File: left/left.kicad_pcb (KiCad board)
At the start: 2 copper layers, 163.9 x 104.5 mm, 51 parts, among them J1 Modulo-Jack, J2 Modulo-Jack, J3 Modulo-Jack, SW1 SW_Push, SW10 SW_Push, SW11 SW_Push, SW12 SW_Push, SW13 SW_Push, SW14 SW_Push, SW15 SW_Push, SW16 SW_Push, SW17 SW_Push, SW18 SW_Push, SW19 SW_Push, SW2 SW_Push, SW20 SW_Push, SW21 SW_Push, SW22 SW_Push, SW23 SW_Push, SW24 SW_Push, SW25 SW_Push, SW26 SW_Push, SW27 SW_Push, SW28 SW_Push, SW29 SW_Push, SW3 SW_Push, SW30 SW_Push, SW31 SW_Push, SW32 SW_SPDT, SW33 SW_SPDT, SW4 SW_Push, SW5 SW_Push, SW6 SW_Push, SW7 SW_Push, SW8 SW_Push, SW9 SW_Push, U1 MCP23017_SP, U2 MCP23017_SP

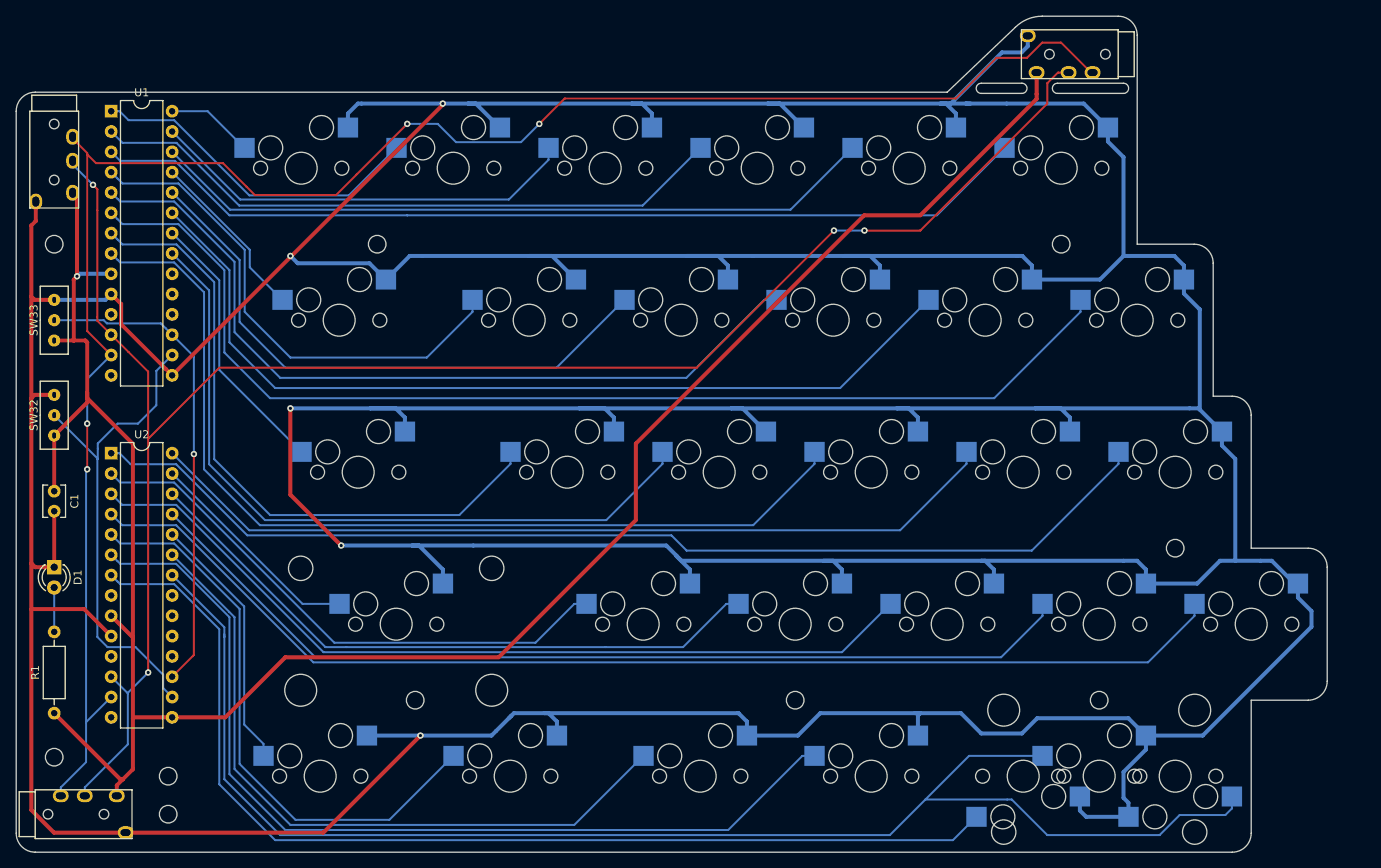
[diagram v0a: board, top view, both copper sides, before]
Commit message: left: change address switch to DPDT
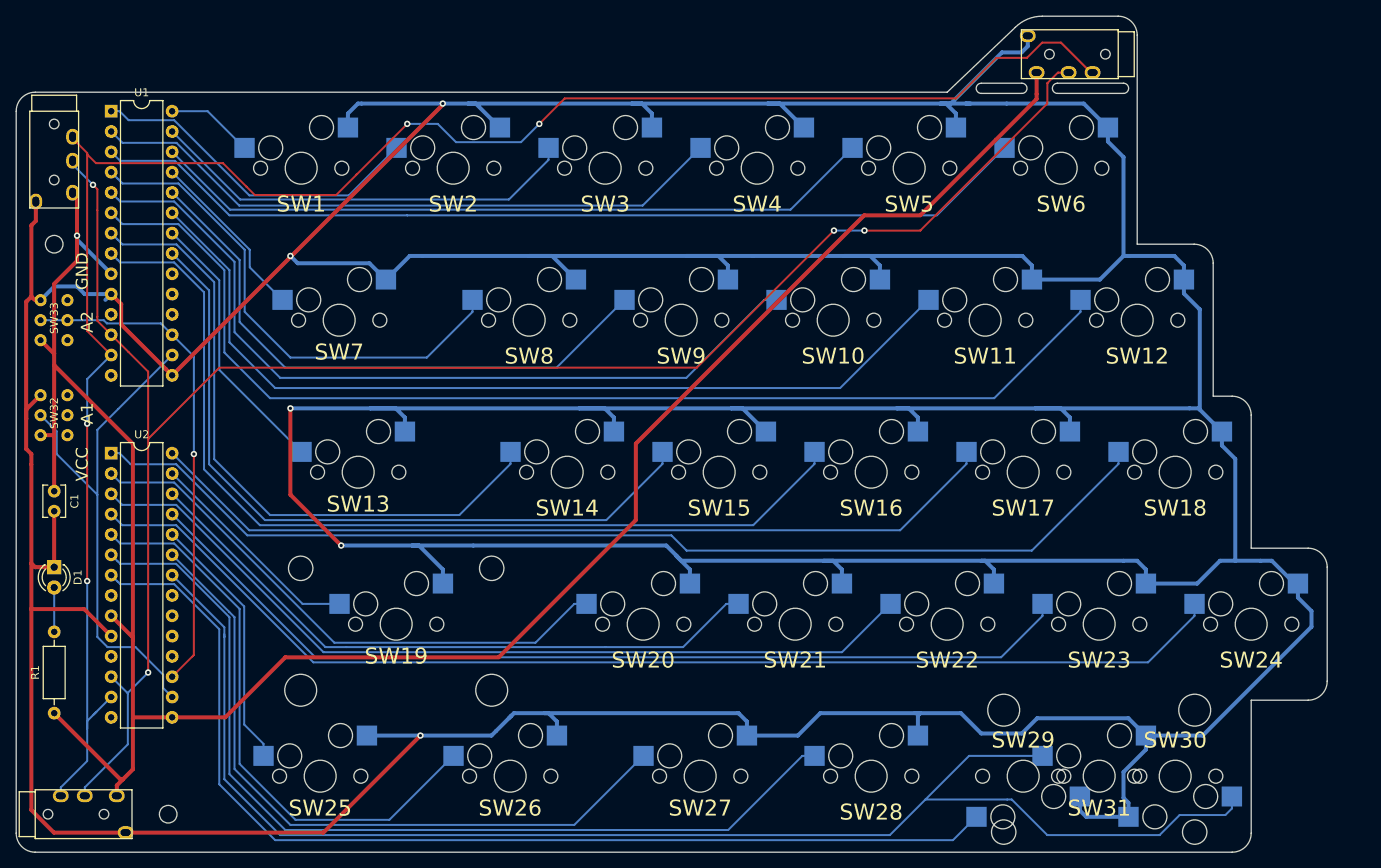
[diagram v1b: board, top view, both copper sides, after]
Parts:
- removed the ? at (190.0, 133.0)
- removed the ? at (59.4, 140.1)
- removed the ? at (73.6, 142.5)
- removed the ? at (104.5, 133.0)
- removed the ? at (99.8, 76.0)
- removed the ? at (185.2, 76.0)
- removed the ? at (199.5, 114.0)
- removed the ? at (152.0, 133.0)
- SW32, SW33: value SW_SPDT -> SW_DPDT_x2; footprint lib:SlideSwitch_SS-12D00 -> lib:SlideSwitch_IS2235
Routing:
- net VCC: track 271.5 -> 278.3 mm
- net A1: track 61.7 -> 65.4 mm
- net GND: track 1029.5 -> 1031.7 mm
- net A2: track 60.5 -> 62.2 mm
- net SDA: track 230.5 -> 231.7 mm
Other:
- board text added: "A1"
- board text added: "A2"
- board text added: "GND"
- board text added: "VCC"

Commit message: left: ネジ穴を再生
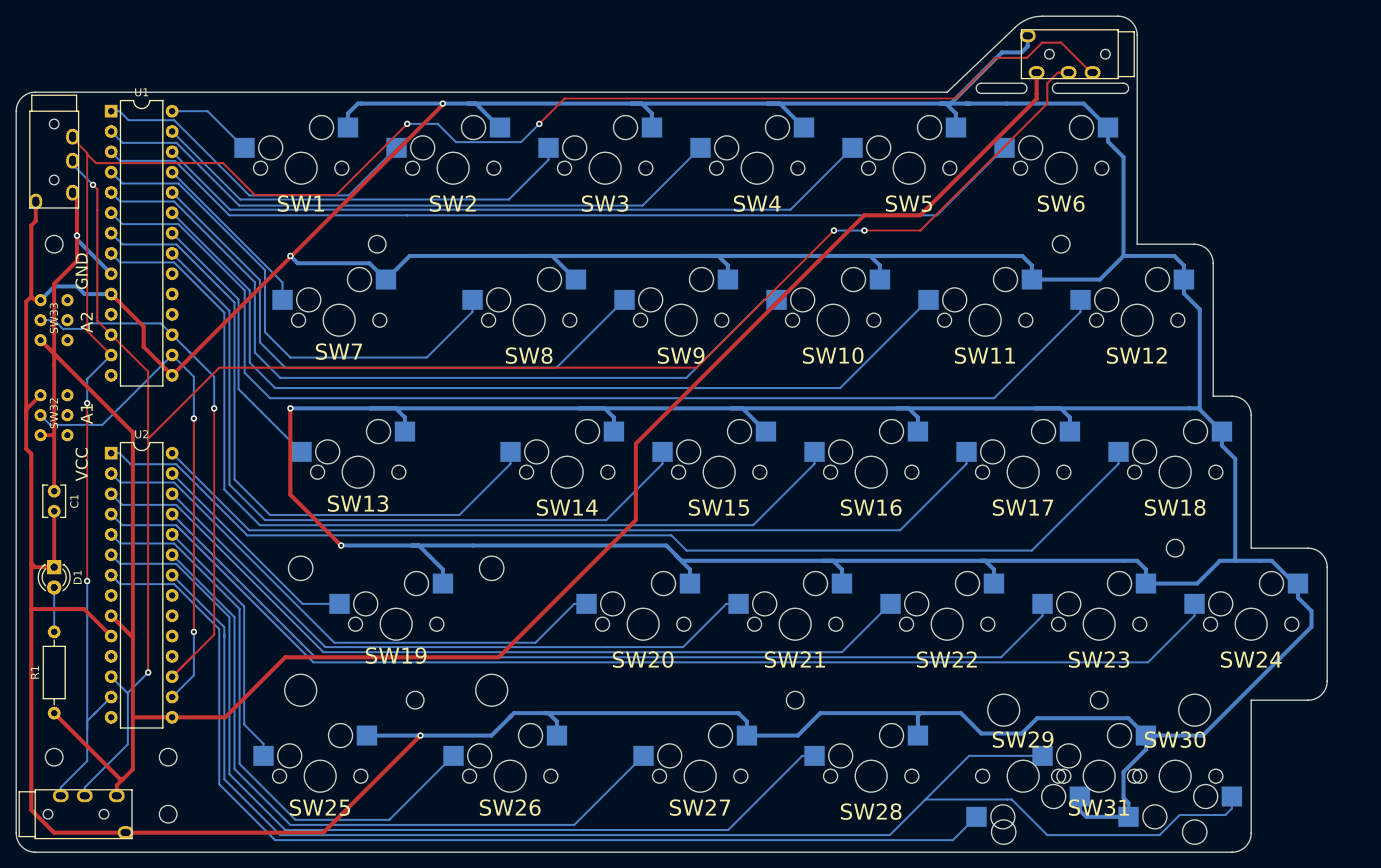
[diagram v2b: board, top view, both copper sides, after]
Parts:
- added ?: M2, lib:MountingHole_2.2mm_M2, F.Cu at (190.0, 133.0)
- added ?: M2, lib:MountingHole_2.2mm_M2, F.Cu at (185.2, 76.0)
- added ?: M2, lib:MountingHole_2.2mm_M2, F.Cu at (199.5, 114.0)
- added ?: M2, lib:MountingHole_2.2mm_M2, F.Cu at (152.0, 133.0)
- added ?: M2, lib:MountingHole_2.2mm_M2, F.Cu at (104.5, 133.0)
- added ?: M2, lib:MountingHole_2.2mm_M2, F.Cu at (99.8, 76.0)
- added ?: M2, lib:MountingHole_2.2mm_M2, F.Cu at (59.4, 140.1)
- added ?: M2, lib:MountingHole_2.2mm_M2, F.Cu at (73.6, 140.1)
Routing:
- net A2: track 62.2 -> 69.5 mm
- net VCC: track 278.3 -> 282.4 mm
- net GND: track 1031.7 -> 1030.7 mm
- net A1: track 65.4 -> 65.6 mm, vias 0 -> 2

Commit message: last commit
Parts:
- added ?: M2, lib:MountingHole_2.2mm_M2, F.Cu at (78.4, 61.8)
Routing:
- net SW1: track 10.9 -> 12.3 mm
- net GND: track 1030.7 -> 1030.2 mm
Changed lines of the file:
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@@
     (thickness 1.6)
     (drawings 37)
-    (tracks 549)
+    (tracks 550)
     (zones 0)
-    (modules 51)
+    (modules 52)
     (nets 56)
   )
@@
   )
   (module lib:MountingHole_2.2mm_M2 locked (layer F.Cu)
+    (at 78.375 61.75)
+    (descr "Mounting Hole 2.2mm, no annular, M2")
+    (tags "mounting hole 2.2mm no annular m2")
+    (attr virtual)
+    (fp_text reference "" (at 0 -3.2) (layer F.SilkS)
+      (effects (font (size 1 1) (thickness 0.15)))
+    )
+    (fp_text value M2 (at 0 3.2) (layer F.Fab)
+      (effects (font (size 1 1) (thickness 0.15)))
+    )
+    (fp_circle (center 0 0) (end 1.75 0) (layer F.CrtYd) (width 0.05))
+    (fp_text user %R (at 0.3 0) (layer F.Fab)
+      (effects (font (size 1 1) (thickness 0.15)))
+    )
+    (pad 1 np_thru_hole circle (at 0 0) (size 2.2 2.2) (drill 2.2) (layers *.Cu *.Mask))
+  )
+  (module lib:MountingHole_2.2mm_M2 locked (layer F.Cu)
     (at 190 133)
     (descr "Mounting Hole 2.2mm, no annular, M2")
@@
   (segment (start 56.515 146.719002) (end 56.515 121.61) (width 0.5) (layer F.Cu) (net 1))
   (segment (start 59.375 109.375) (end 59.375 116.375) (width 0.5) (layer F.Cu) (net 1))
-  (segment (start 214.842 120.17) (end 214.842 118.42) (width 0.5) (layer B.Cu) (net 1))
-  (segment (start 216.535 121.863) (end 214.842 120.17) (width 0.5) (layer B.Cu) (net 1))
-  (segment (start 216.535 123.825) (end 216.535 121.863) (width 0.5) (layer B.Cu) (net 1))
-  (segment (start 195.842 137.42) (end 202.94 137.42) (width 0.5) (layer B.Cu) (net 1))
-  (segment (start 202.94 137.42) (end 216.535 123.825) (width 0.5) (layer B.Cu) (net 1))
   (segment (start 188.067 58.42) (end 178.435 58.42) (width 0.5) (layer B.Cu) (net 1))
   (segment (start 191.067 61.42) (end 188.067 58.42) (width 0.5) (layer B.Cu) (net 1))
@@
   (segment (start 66.5 82.235) (end 70.555 86.29) (width 0.5) (layer F.Cu) (net 1))
   (segment (start 70.555 88.83) (end 73.320001 91.595001) (width 0.5) (layer F.Cu) (net 1))
+  (segment (start 214.842 120.17) (end 214.842 118.42) (width 0.5) (layer B.Cu) (net 1))
+  (segment (start 215.9 121.228) (end 214.842 120.17) (width 0.5) (layer B.Cu) (net 1))
+  (segment (start 215.9 124.46) (end 215.9 121.228) (width 0.5) (layer B.Cu) (net 1))
+  (segment (start 202.94 137.42) (end 215.9 124.46) (width 0.5) (layer B.Cu) (net 1))
+  (segment (start 195.842 137.42) (end 202.94 137.42) (width 0.5) (layer B.Cu) (net 1))
   (segment (start 67.2 143.65) (end 67.2 144.95) (width 0.5) (layer F.Cu) (net 2))
   (segment (start 69.215 135.255) (end 69.325 135.145) (width 0.5) (layer F.Cu) (net 2))
@@
   (segment (start 160.655 74.295) (end 167.64 74.295) (width 0.25) (layer F.Cu) (net 4))
   (segment (start 167.64 74.295) (end 183.515 58.42) (width 0.25) (layer F.Cu) (net 4))
-  (segment (start 78.555 59.375) (end 74.12 59.375) (width 0.25) (layer B.Cu) (net 5))
-  (segment (start 83.165 63.96) (end 83.14 63.96) (width 0.25) (layer B.Cu) (net 5))
-  (segment (start 83.14 63.96) (end 78.555 59.375) (width 0.25) (layer B.Cu) (net 5))
+  (segment (start 83.165 63.96) (end 83.165 61.615) (width 0.25) (layer B.Cu) (net 5))
+  (segment (start 80.925 59.375) (end 77.79 59.375) (width 0.25) (layer B.Cu) (net 5))
+  (segment (start 83.165 61.615) (end 80.925 59.375) (width 0.25) (layer B.Cu) (net 5))
+  (segment (start 77.79 59.375) (end 74.12 59.375) (width 0.25) (layer B.Cu) (net 5))
   (segment (start 102.14 63.96) (end 102.165 63.96) (width 0.25) (layer B.Cu) (net 6))
   (segment (start 66.5 59.375) (end 67.55 59.375) (width 0.25) (layer B.Cu) (net 6))

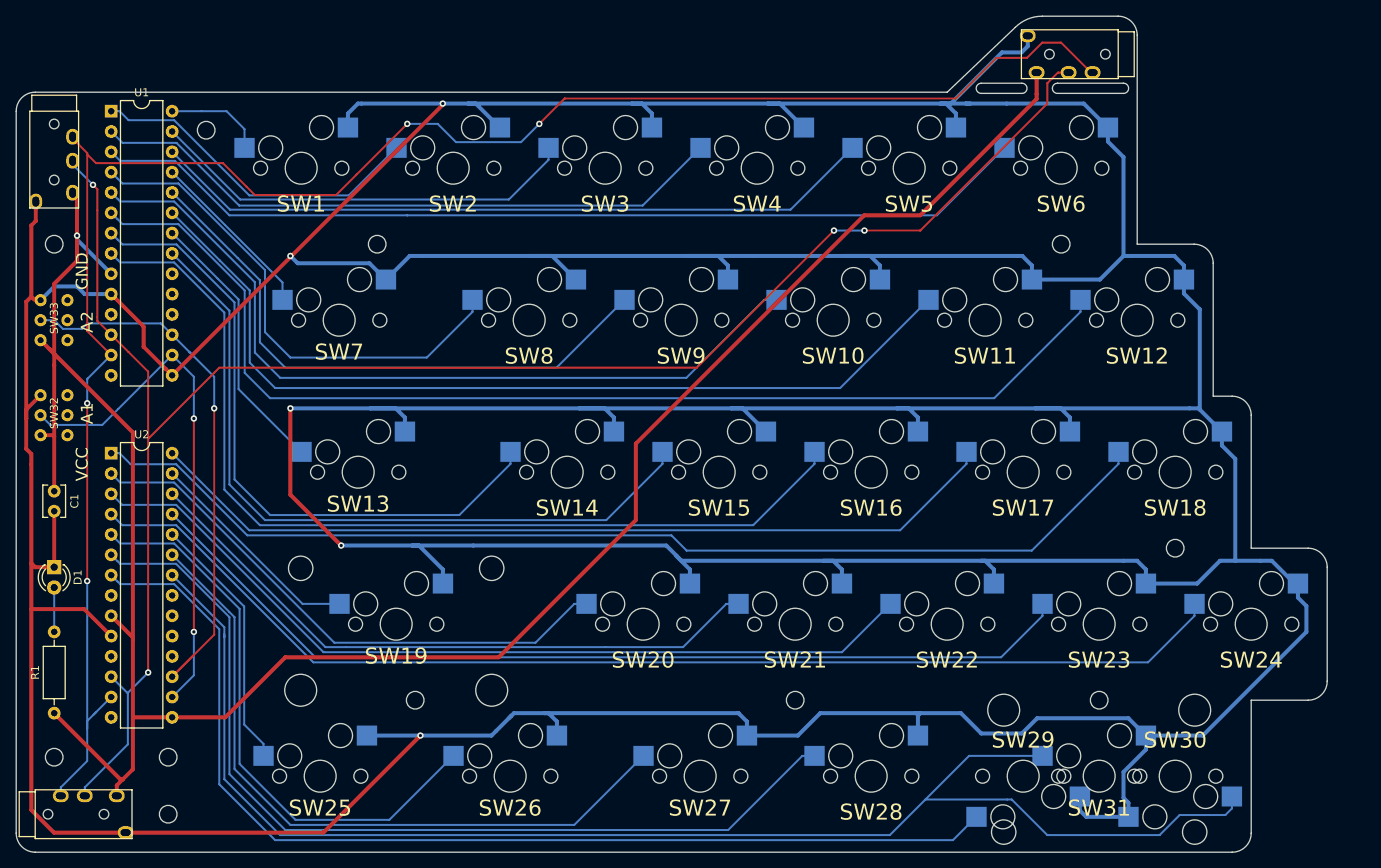
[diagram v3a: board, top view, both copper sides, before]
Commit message: modify left to JIS layout
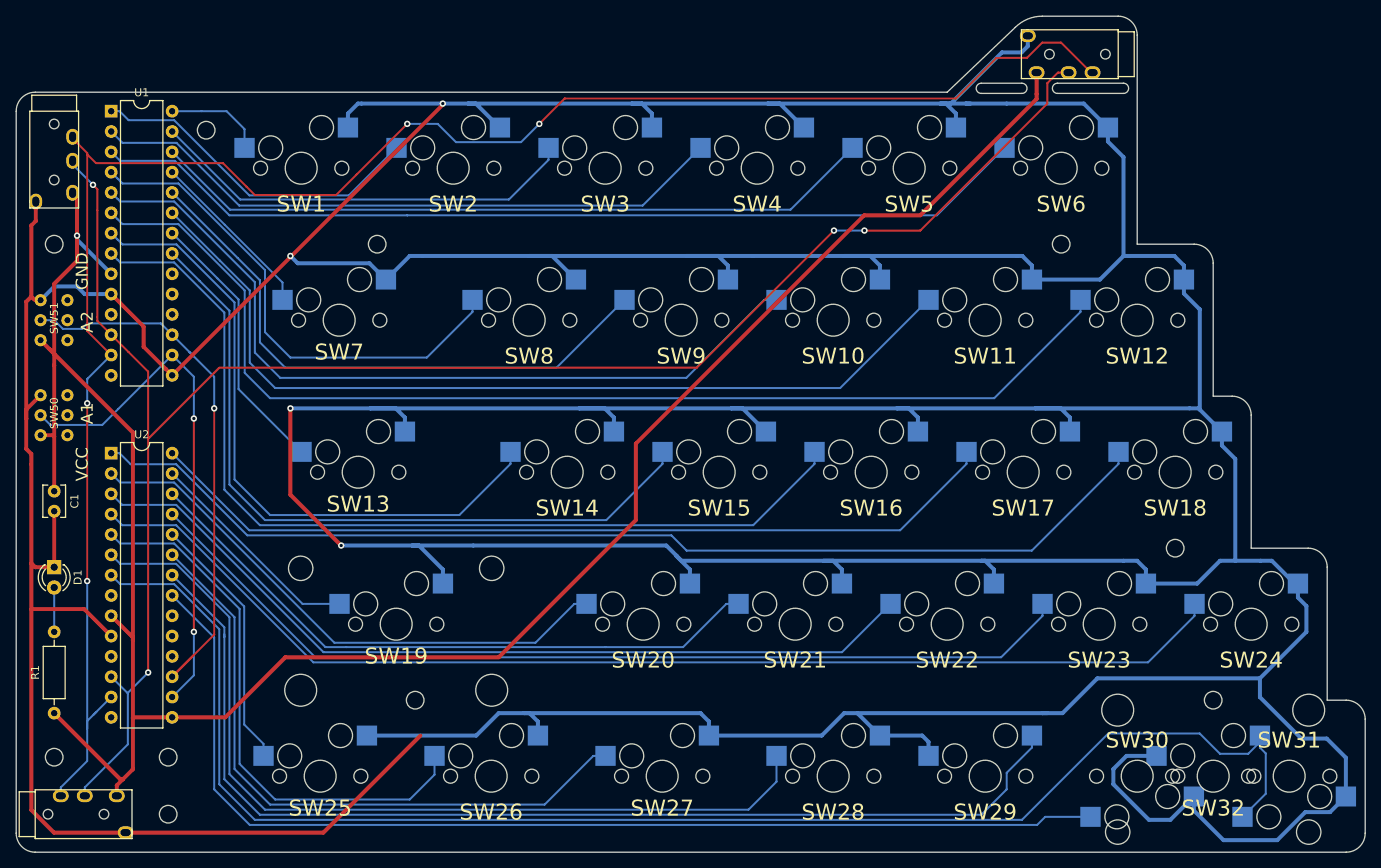
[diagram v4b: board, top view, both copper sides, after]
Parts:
- removed the ? at (190.0, 133.0)
- removed SW33: SW_DPDT_x2, lib:SlideSwitch_IS2235
- added SW50: SW_DPDT_x2, lib:SlideSwitch_IS2235, F.Cu at (59.4, 97.4)
- added SW51: SW_DPDT_x2, lib:SlideSwitch_IS2235, F.Cu at (59.4, 85.5)
- SW26: footprint MX_Socket:MXOnly-1.25U-Hotswap -> MX_Socket:MXOnly-1U-Hotswap
- SW31: footprint MX_Socket:MXOnly-2U-Hotswap-ReversedStabilizers -> MX_Socket:MXOnly-1U-Hotswap
- SW32: value SW_DPDT_x2 -> SW_Push; footprint lib:SlideSwitch_IS2235 -> MX_Socket:MXOnly-2U-Hotswap-ReversedStabilizers
- moved SW32 151.7 mm to (204.2, 142.5), turned to 0 degrees
- moved ? 52.2 mm to (204.2, 133.0)
- moved SW31 23.8 mm to (213.8, 142.5), turned to 180 degrees
- moved SW27 4.75 mm to (135.4, 142.5)
- moved SW28 4.75 mm to (156.8, 142.5)
- moved SW29 4.75 mm to (175.8, 142.5), turned to 0 degrees
- moved SW30 4.75 mm to (194.8, 142.5)
- moved SW26 2.38 mm to (114.0, 142.5)
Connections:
- SW30 pad 1: SW30 -> GND
- SW30 pad 2: GND -> SW30
- SW31 pad 1: SW30 -> GND
- SW31 pad 2: GND -> SW31
- SW32 pad 1: VCC -> GND
- SW32 pad 2: A1 -> SW31
- U2 pad 21: Net-(U2-Pad21) -> SW30
- U2 pad 22: SW30 -> SW29
- U2 pad 7: SW29 -> SW31
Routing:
- net SW31: track 0.00 -> 186.0 mm
- net GND: track 1030.2 -> 1082.2 mm, vias 5 -> 4
- net SW30: track 180.8 -> 138.2 mm
- net SW27: track 87.6 -> 80.7 mm
- net SW28: track 117.5 -> 112.5 mm
- net SW26: track 72.2 -> 69.1 mm
- net SW29: track 134.4 -> 137.5 mm
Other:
- board size 163.9 x 104.5 mm -> 168.6 x 104.5 mm

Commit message: modify mounting holl
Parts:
- added ?: M2, lib:MountingHole_2.2mm_M2, F.Cu at (166.2, 133.0)
- moved ? 28.5 mm to (128.2, 76.0)
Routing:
- net GND: track 1082.2 -> 1070.6 mm
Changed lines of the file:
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@@
     (thickness 1.6)
     (drawings 37)
-    (tracks 559)
+    (tracks 563)
     (zones 0)
-    (modules 52)
+    (modules 53)
     (nets 56)
   )
@@
     (add_net VCC)
   )
+  (module lib:MountingHole_2.2mm_M2 locked (layer F.Cu)
+    (at 166.25 133)
+    (descr "Mounting Hole 2.2mm, no annular, M2")
+    (tags "mounting hole 2.2mm no annular m2")
+    (attr virtual)
+    (fp_text reference "" (at 0 -3.2) (layer F.SilkS)
+      (effects (font (size 1 1) (thickness 0.15)))
+    )
+    (fp_text value M2 (at 0 3.2) (layer F.Fab)
+      (effects (font (size 1 1) (thickness 0.15)))
+    )
+    (fp_circle (center 0 0) (end 1.75 0) (layer F.CrtYd) (width 0.05))
+    (fp_text user %R (at 0.3 0) (layer F.Fab)
+      (effects (font (size 1 1) (thickness 0.15)))
+    )
+    (pad 1 np_thru_hole circle (at 0 0) (size 2.2 2.2) (drill 2.2) (layers *.Cu *.Mask))
+  )
   (module lib:SlideSwitch_IS2235 (layer F.Cu)
     (at 59.375 85.5 90)
@@
   )
   (module lib:MountingHole_2.2mm_M2 locked (layer F.Cu)
-    (at 99.75 76)
+    (at 128.25 76)
     (descr "Mounting Hole 2.2mm, no annular, M2")
     (tags "mounting hole 2.2mm no annular m2")
@@
   (segment (start 143.592 80.42) (end 143.592 78.67) (width 0.5) (layer B.Cu) (net 1))
   (segment (start 146.685 77.47) (end 138.43 77.47) (width 0.5) (layer B.Cu) (net 1))
-  (segment (start 138.43 77.47) (end 118.745 77.47) (width 0.5) (layer B.Cu) (net 1))
   (segment (start 161.392 77.47) (end 158.115 77.47) (width 0.5) (layer B.Cu) (net 1))
   (segment (start 162.592 78.67) (end 161.392 77.47) (width 0.5) (layer B.Cu) (net 1))
@@
   (segment (start 182.88 134.62) (end 185.42 134.62) (width 0.5) (layer B.Cu) (net 1))
   (segment (start 182.88 134.62) (end 183.515 134.62) (width 0.5) (layer B.Cu) (net 1))
-  (segment (start 159.767 134.62) (end 182.88 134.62) (width 0.5) (layer B.Cu) (net 1))
   (segment (start 189.772 130.268) (end 210.092 130.268) (width 0.5) (layer B.Cu) (net 1))
   (segment (start 185.42 134.62) (end 189.772 130.268) (width 0.5) (layer B.Cu) (net 1))
+  (segment (start 130.955 80.42) (end 133.905 77.47) (width 0.5) (layer B.Cu) (net 1))
+  (segment (start 124.592 80.42) (end 130.955 80.42) (width 0.5) (layer B.Cu) (net 1))
+  (segment (start 138.43 77.47) (end 133.905 77.47) (width 0.5) (layer B.Cu) (net 1))
+  (segment (start 167.875 137.42) (end 168.015 137.42) (width 0.5) (layer B.Cu) (net 1))
+  (segment (start 168.015 137.42) (end 170.815 134.62) (width 0.5) (layer B.Cu) (net 1))
+  (segment (start 170.815 134.62) (end 182.88 134.62) (width 0.5) (layer B.Cu) (net 1))
   (segment (start 67.2 143.65) (end 67.2 144.95) (width 0.5) (layer F.Cu) (net 2))
   (segment (start 69.215 135.255) (end 69.325 135.145) (width 0.5) (layer F.Cu) (net 2))
